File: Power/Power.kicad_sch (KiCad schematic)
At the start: 55 parts, among them J1 Conn_01x04_Pin, J2 Conn_01x02, J3 Conn_01x06, J4 Conn_01x07, J5 GND, J6 +BATT, Q2 AO3400A, Q3 AO3400A, Q4 AO3400A, U1 TPS54331DR, U2 XAL4030-682MEC, U3 TPS54331DR, U4 XAL4030-682MEC

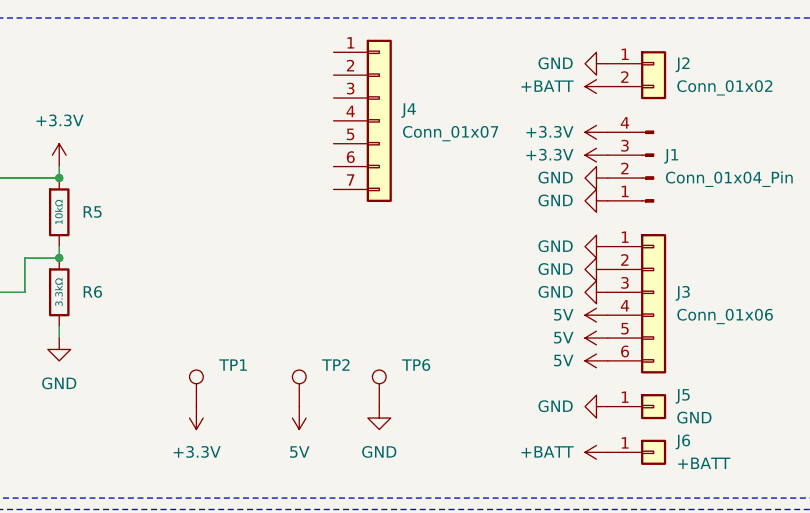
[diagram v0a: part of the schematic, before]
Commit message: feat: Added mounting holes, text and more connectors for PMU
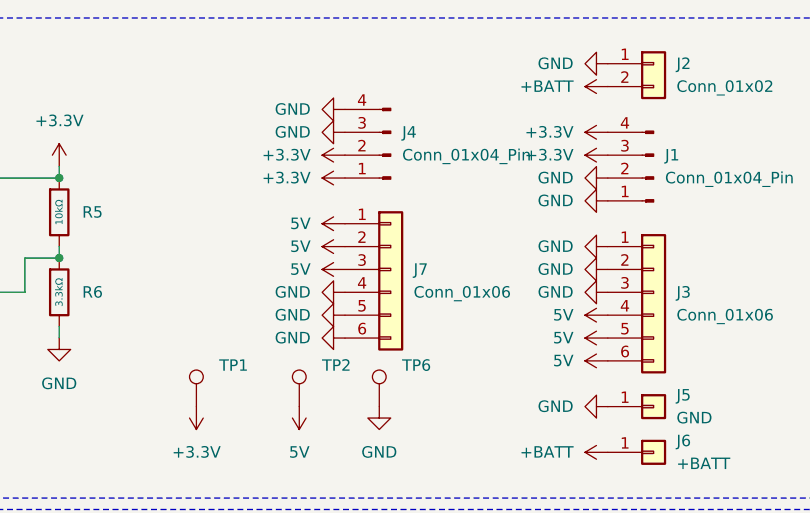
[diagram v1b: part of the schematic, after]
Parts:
- removed J4: Conn_01x07, symbol Connector_Generic:Conn_01x07
- added J4: Conn_01x04_Pin, Connector_JST:JST_GH_SM04B-GHS-TB_1x04-1MP_P1.25mm_Horizontal, symbol Connector:Conn_01x04_Pin
- added J7: Conn_01x06, Connector_JST:JST_GH_SM06B-GHS-TB_1x06-1MP_P1.25mm_Horizontal, symbol Connector_Generic:Conn_01x06
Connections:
- net +3.3V: now also J4.1 (Pin_1), J4.2 (Pin_2)
- net 5V: now also J7.1 (Pin_1), J7.2 (Pin_2), J7.3 (Pin_3)
- net GND: now also J4.3 (Pin_3), J4.4 (Pin_4), J7.4 (Pin_4), J7.5 (Pin_5), J7.6 (Pin_6)
